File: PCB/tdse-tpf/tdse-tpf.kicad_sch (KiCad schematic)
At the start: 10 parts, among them J1 CN7, J2 CN10, J3 Conn_01x04, J4 Conn_01x05, J5 Conn_01x02, J6 Conn_01x16, J7 Conn_01x04

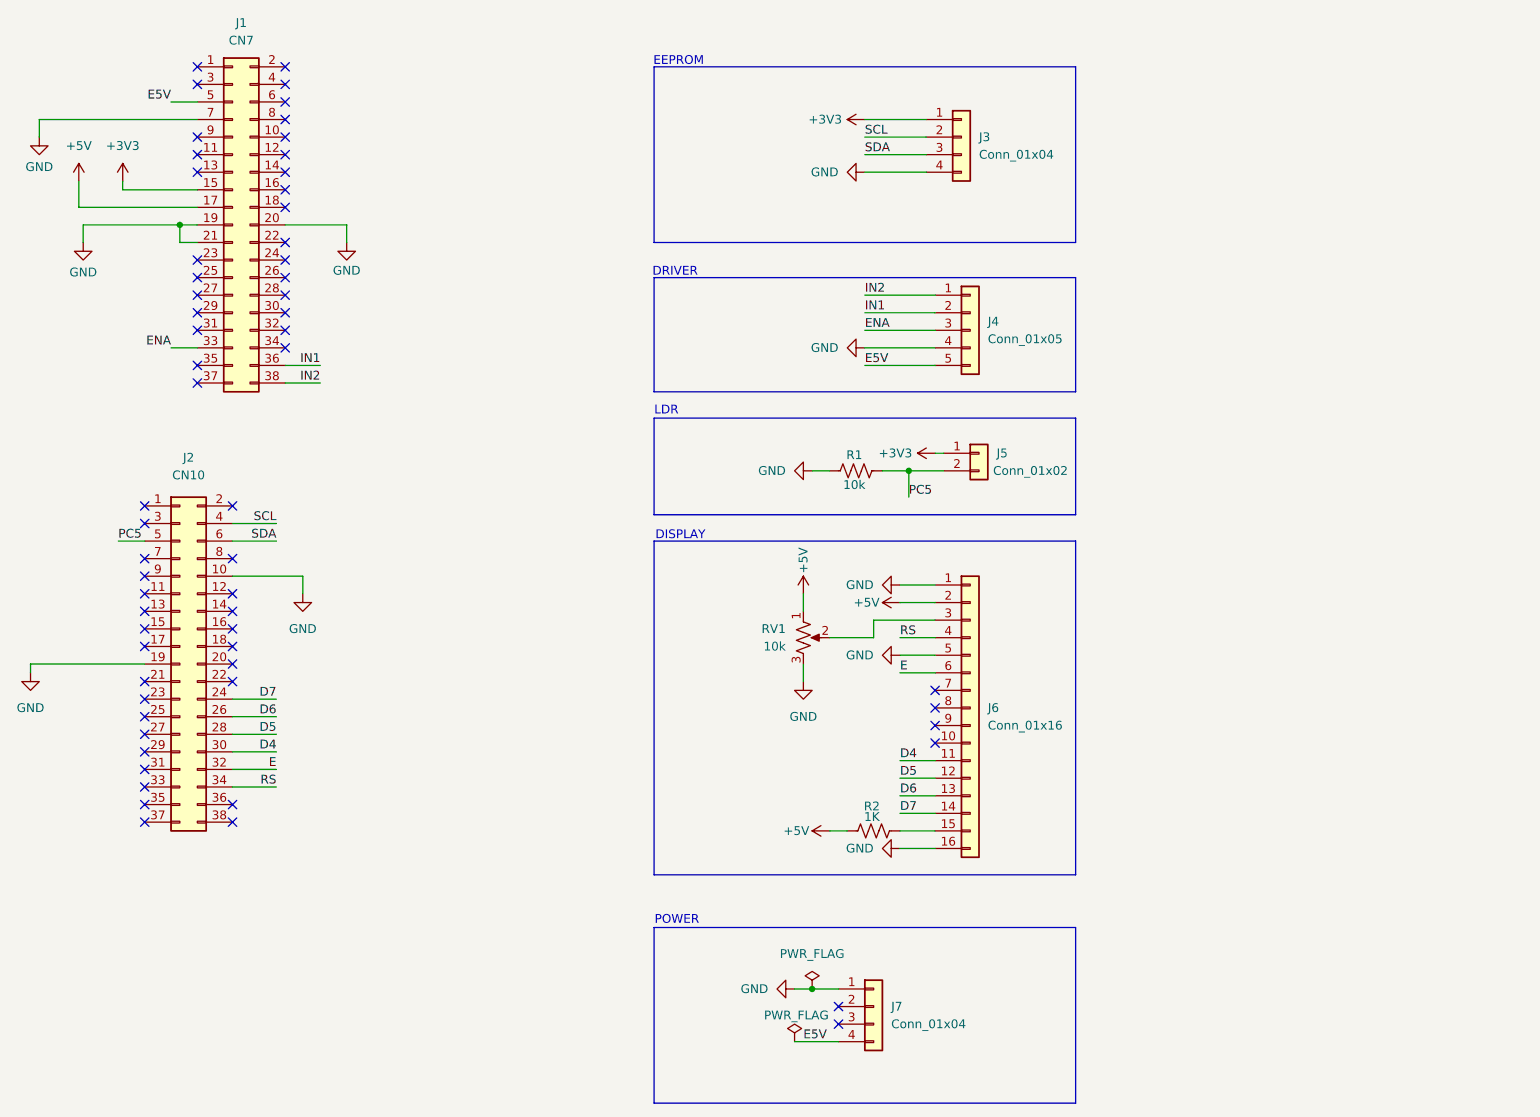
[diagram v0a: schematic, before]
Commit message: Changed pins sensor-ldr-display & updated pcb pads
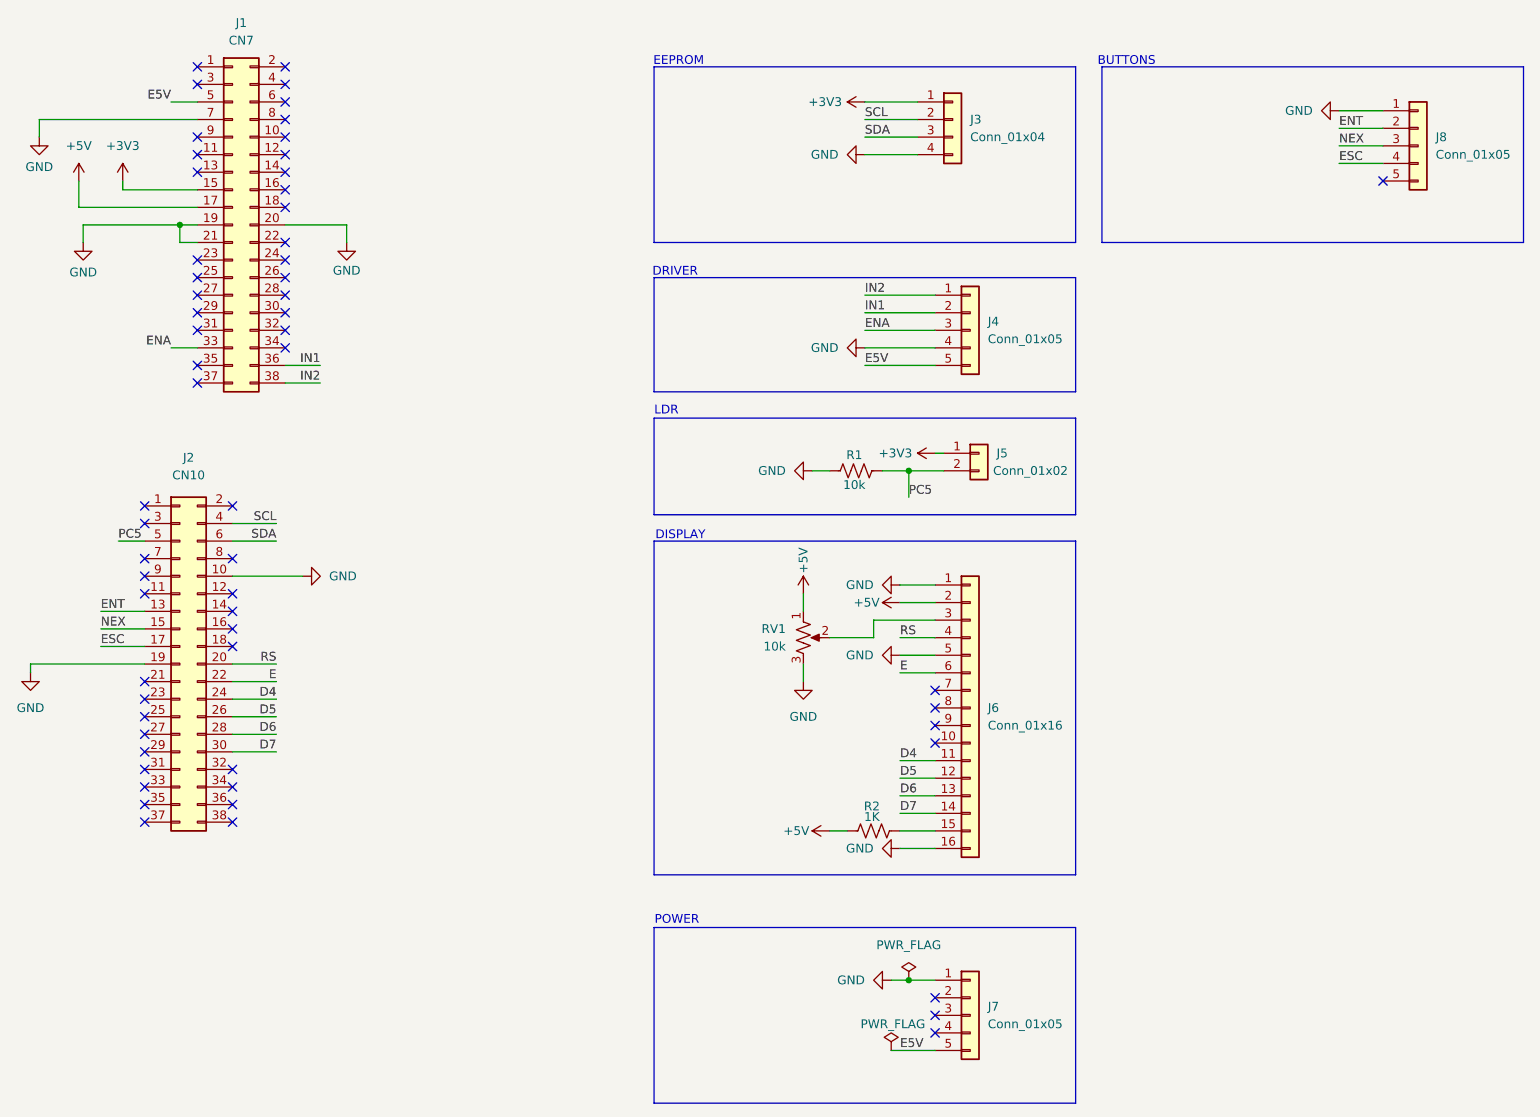
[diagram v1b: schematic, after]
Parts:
- removed J7: Conn_01x04, Connector_PinSocket_2.54mm:PinSocket_1x04_P2.54mm_Vertical, symbol Connector_Generic:Conn_01x04
- added J7: Conn_01x05, Connector_PinSocket_2.54mm:PinSocket_1x05_P2.54mm_Vertical, symbol Connector_Generic:Conn_01x05
- added J8: Conn_01x05, Connector_PinHeader_2.54mm:PinHeader_1x05_P2.54mm_Vertical, symbol Connector_Generic:Conn_01x05
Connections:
- net D4: now also J2.24 (Pin_24); no longer J2.30 (Pin_30)
- net D5: now also J2.26 (Pin_26); no longer J2.28 (Pin_28)
- net D6: now also J2.28 (Pin_28); no longer J2.26 (Pin_26)
- net D7: now also J2.30 (Pin_30); no longer J2.24 (Pin_24)
- net E: now also J2.22 (Pin_22); no longer J2.32 (Pin_32)
- net E5V: now also J7.5 (Pin_5)
- net GND: now also J7.1 (Pin_1), J8.1 (Pin_1)
- net RS: now also J2.20 (Pin_20); no longer J2.34 (Pin_34)
- net ENT: now reaches J2.13 (Pin_13)
- net ENT: now also J8.2 (Pin_2)
- net NEX: now reaches J2.15 (Pin_15)
- net NEX: now also J8.3 (Pin_3)
- net ESC: now reaches J2.17 (Pin_17)
- net ESC: now also J8.4 (Pin_4)
- no-connect marks 61 -> 60
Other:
- note added: "BUTTONS"
- moved on the sheet: J3
